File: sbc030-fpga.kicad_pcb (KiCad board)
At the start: 4 copper layers, 152.4 x 114.3 mm, 10 parts, among them J100 C96, U200 74LVC245, U201 74LVC245, U202 74LVC245, U203 74LVC245, U210 74LVC245, U211 74LVC245, U212 74LVC245, U213 74LVC245, U300 LFE5U

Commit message: use LFE5U-12F-8BG256C schematic symbol
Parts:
- U300: value LFE5U -> LFE5U-12F-8BG256C
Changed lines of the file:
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@@
       (effects (font (size 1 1) (thickness 0.15)))
     )
-    (fp_text value LFE5U (at 0 8.2) (layer F.Fab)
+    (fp_text value LFE5U-12F-8BG256C (at 0 8.2) (layer F.Fab)
       (effects (font (size 1 1) (thickness 0.15)))
     )

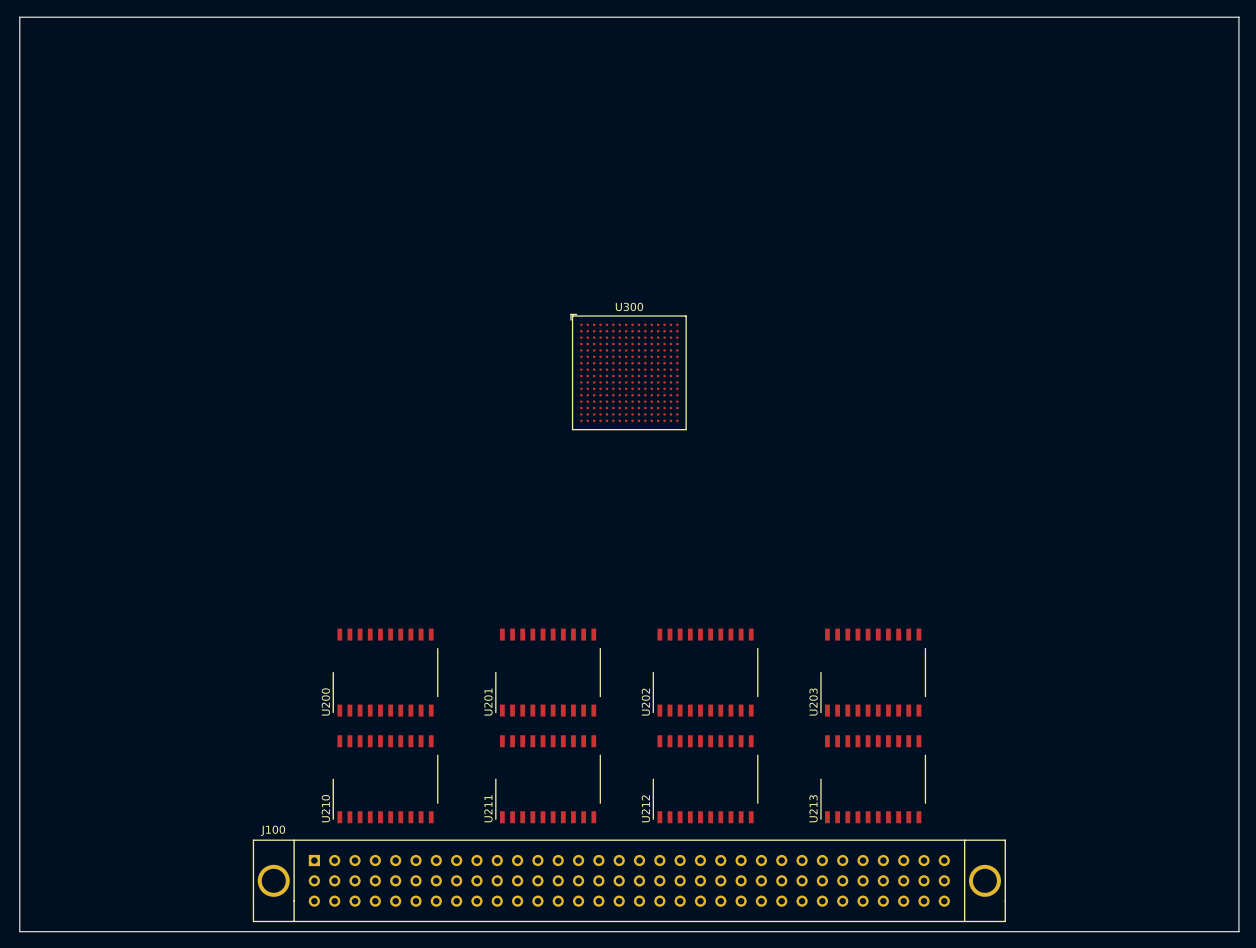
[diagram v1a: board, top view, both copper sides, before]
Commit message: updated schematic and initial bga fanout
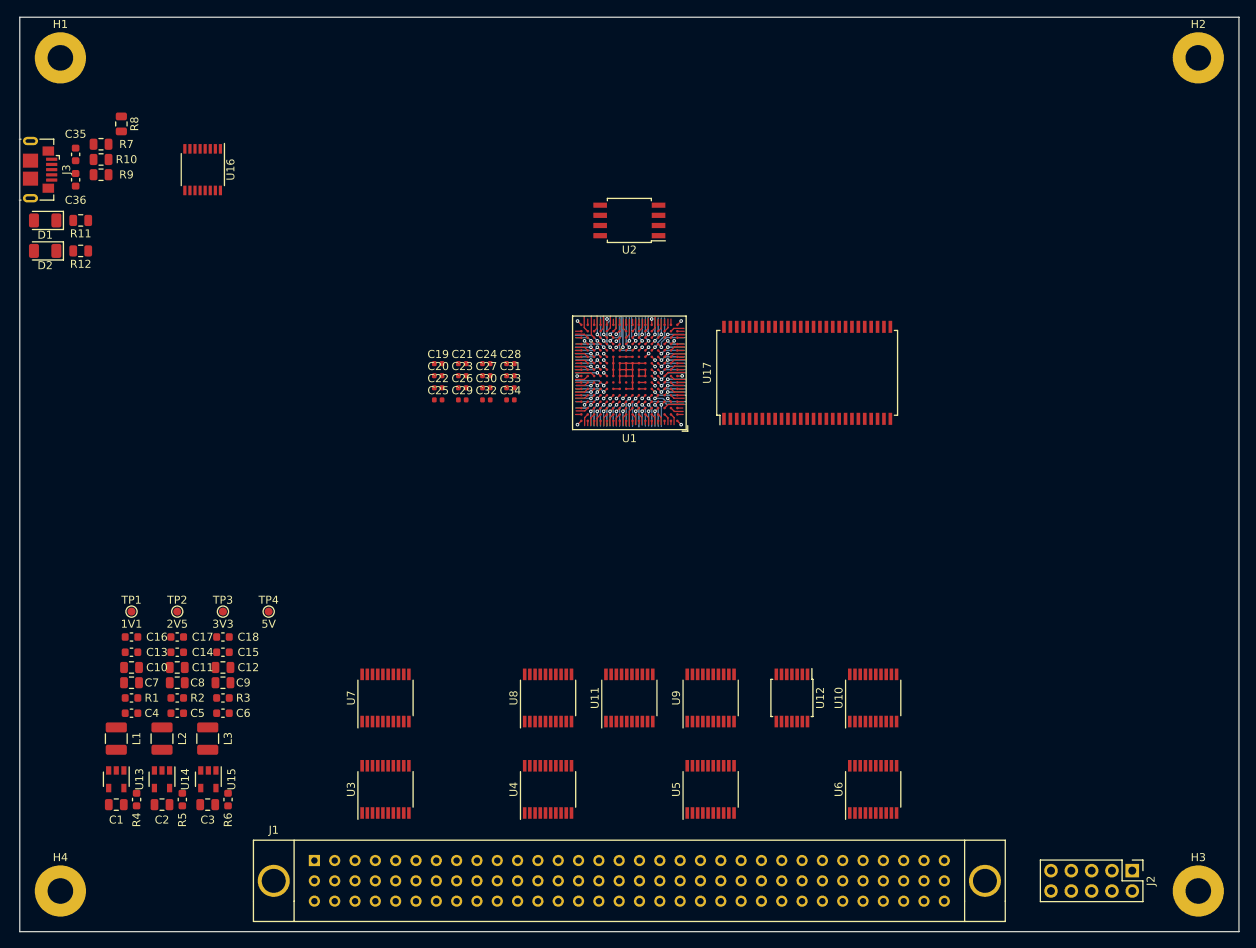
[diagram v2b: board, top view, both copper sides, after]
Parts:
- removed J100: C96, parts:C96ABCM
- removed U200, U201, U202, U203, U210, U211, U212, U213: 74LVC245, Package_SO:SO-20_12.8x7.5mm_P1.27mm
- removed U300: LFE5U-12F-8BG256C, Package_BGA:BGA-256_14.0x14.0mm_Layout16x16_P0.8mm_Ball0.45mm_Pad0.32mm_NSMD
- added C1: 22uF, Capacitor_SMD:C_0805_2012Metric, F.Cu at (81.9, 130.2)
- added C10: 22uF, Capacitor_SMD:C_0805_2012Metric, F.Cu at (83.8, 113.0)
- added C11: 22uF, Capacitor_SMD:C_0805_2012Metric, F.Cu at (89.5, 113.0)
- added C12: 22uF, Capacitor_SMD:C_0805_2012Metric, F.Cu at (95.2, 113.0)
- added C13: 2.2uF, Capacitor_SMD:C_0603_1608Metric, F.Cu at (83.8, 111.1)
- added C14: 2.2uF, Capacitor_SMD:C_0603_1608Metric, F.Cu at (89.5, 111.1)
- added C15: 2.2uF, Capacitor_SMD:C_0603_1608Metric, F.Cu at (95.2, 111.1)
- added C16: 2.2uF, Capacitor_SMD:C_0603_1608Metric, F.Cu at (83.8, 109.2)
- added C17: 2.2uF, Capacitor_SMD:C_0603_1608Metric, F.Cu at (89.5, 109.2)
- added C18: 2.2uF, Capacitor_SMD:C_0603_1608Metric, F.Cu at (95.2, 109.2)
- added C19: 22nF, Capacitor_SMD:C_0402_1005Metric, F.Cu at (122.2, 75.1)
- added C2: 22uF, Capacitor_SMD:C_0805_2012Metric, F.Cu at (87.6, 130.2)
- added C20: 22nF, Capacitor_SMD:C_0402_1005Metric, F.Cu at (122.2, 76.6)
- added C21: 22nF, Capacitor_SMD:C_0402_1005Metric, F.Cu at (125.2, 75.1)
- added C22: 22nF, Capacitor_SMD:C_0402_1005Metric, F.Cu at (122.2, 78.1)
- added C23: 22nF, Capacitor_SMD:C_0402_1005Metric, F.Cu at (125.2, 76.6)
- added C24: 22nF, Capacitor_SMD:C_0402_1005Metric, F.Cu at (128.2, 75.1)
- added C25: 22nF, Capacitor_SMD:C_0402_1005Metric, F.Cu at (122.2, 79.6)
- added C26: 22nF, Capacitor_SMD:C_0402_1005Metric, F.Cu at (125.2, 78.1)
- added C27: 22nF, Capacitor_SMD:C_0402_1005Metric, F.Cu at (128.2, 76.6)
- added C28: 22nF, Capacitor_SMD:C_0402_1005Metric, F.Cu at (131.2, 75.1)
- added C29: 22nF, Capacitor_SMD:C_0402_1005Metric, F.Cu at (125.2, 79.6)
- added C3: 22uF, Capacitor_SMD:C_0805_2012Metric, F.Cu at (93.3, 130.2)
- added C30: 22nF, Capacitor_SMD:C_0402_1005Metric, F.Cu at (128.2, 78.1)
- added C31: 22nF, Capacitor_SMD:C_0402_1005Metric, F.Cu at (131.2, 76.6)
- added C32: 22nF, Capacitor_SMD:C_0402_1005Metric, F.Cu at (128.2, 79.6)
- added C33: 22nF, Capacitor_SMD:C_0402_1005Metric, F.Cu at (131.2, 78.1)
- added C34: 22nF, Capacitor_SMD:C_0402_1005Metric, F.Cu at (131.2, 79.6)
- added C35: 47pF, Capacitor_SMD:C_0603_1608Metric, F.Cu at (76.8, 48.9)
- added C36: 47pF, Capacitor_SMD:C_0603_1608Metric, F.Cu at (76.8, 52.1)
- added C4: 470pF, Capacitor_SMD:C_0603_1608Metric, F.Cu at (83.8, 118.7)
- added C5: 470pF, Capacitor_SMD:C_0603_1608Metric, F.Cu at (89.5, 118.7)
- added C6: 470pF, Capacitor_SMD:C_0603_1608Metric, F.Cu at (95.2, 118.7)
- added C7: 22uF, Capacitor_SMD:C_0805_2012Metric, F.Cu at (83.8, 114.9)
- added C8: 22uF, Capacitor_SMD:C_0805_2012Metric, F.Cu at (89.5, 114.9)
- added C9: 22uF, Capacitor_SMD:C_0805_2012Metric, F.Cu at (95.2, 114.9)
- added D1: LED, LED_SMD:LED_1206_3216Metric, F.Cu at (73.0, 57.1)
- added D2: LED, LED_SMD:LED_1206_3216Metric, F.Cu at (73.0, 61.0)
- added H1: MountingHole, MountingHole:MountingHole_3.2mm_M3, F.Cu at (74.9, 36.8)
- added H2: MountingHole, MountingHole:MountingHole_3.2mm_M3, F.Cu at (217.2, 36.8)
- added H3: MountingHole, MountingHole:MountingHole_3.2mm_M3, F.Cu at (217.2, 141.0)
- added H4: MountingHole, MountingHole:MountingHole_3.2mm_M3, F.Cu at (74.9, 141.0)
- added J1: C96, parts:C96ABCM, F.Cu at (106.7, 137.2)
- added J2: JTAG, Connector_PinHeader_2.54mm:PinHeader_2x05_P2.54mm_Vertical, F.Cu at (208.9, 138.4)
- added J3: USB_B_Micro, Connector_USB:USB_Micro-B_GCT_USB3076-30-A, F.Cu at (72.4, 50.8)
- added L1: 2.2uH, Inductor_SMD:L_1210_3225Metric, F.Cu at (81.9, 121.9)
- added L2: 2.2uH, Inductor_SMD:L_1210_3225Metric, F.Cu at (87.6, 121.9)
- added L3: 2.2uH, Inductor_SMD:L_1210_3225Metric, F.Cu at (93.3, 121.9)
- added R1: 15K, Resistor_SMD:R_0603_1608Metric, F.Cu at (83.8, 116.8)
- added R10: 27R, Resistor_SMD:R_0805_2012Metric, F.Cu at (80.0, 49.5)
- added R11: 10K, Resistor_SMD:R_0805_2012Metric, F.Cu at (77.5, 57.1)
- added R12: 10K, Resistor_SMD:R_0805_2012Metric, F.Cu at (77.5, 61.0)
- added R2: 15K, Resistor_SMD:R_0603_1608Metric, F.Cu at (89.5, 116.8)
- added R3: 15K, Resistor_SMD:R_0603_1608Metric, F.Cu at (95.2, 116.8)
- added R4: 18K, Resistor_SMD:R_0603_1608Metric, F.Cu at (84.5, 129.5)
- added R5: 4.7K, Resistor_SMD:R_0603_1608Metric, F.Cu at (90.2, 129.5)
- added R6: 3.3K, Resistor_SMD:R_0603_1608Metric, F.Cu at (95.9, 129.5)
- added R7: 4.7K, Resistor_SMD:R_0805_2012Metric, F.Cu at (80.0, 47.6)
- added R8: 10K, Resistor_SMD:R_0805_2012Metric, F.Cu at (82.5, 45.1)
- added R9: 27R, Resistor_SMD:R_0805_2012Metric, F.Cu at (80.0, 51.4)
- added TP1: 1V1, TestPoint:TestPoint_Pad_D1.0mm, F.Cu at (83.8, 106.0)
- added TP2: 2V5, TestPoint:TestPoint_Pad_D1.0mm, F.Cu at (89.5, 106.0)
- added TP3: 3V3, TestPoint:TestPoint_Pad_D1.0mm, F.Cu at (95.2, 106.0)
- added TP4: 5V, TestPoint:TestPoint_Pad_D1.0mm, F.Cu at (101.0, 106.0)
- added U1: LFE5U-12F-8BG256C, Package_BGA:BGA-256_14.0x14.0mm_Layout16x16_P0.8mm_Ball0.45mm_Pad0.32mm_NSMD, F.Cu at (146.1, 76.2)
- added U10: 74LVC245, Package_SO:TSSOP-20_4.4x6.5mm_P0.65mm, F.Cu at (176.5, 116.8)
- added U11: 74LVC245, Package_SO:TSSOP-20_4.4x6.5mm_P0.65mm, F.Cu at (146.1, 116.8)
- added U12: TXS0104E, Package_SO:TSSOP-14_4.4x5mm_P0.65mm, F.Cu at (166.4, 116.8)
- added U13: TLV62569DBVR, Package_TO_SOT_SMD:SOT-23-5, F.Cu at (81.9, 127.0)
- added U14: TLV62569DBVR, Package_TO_SOT_SMD:SOT-23-5, F.Cu at (87.6, 127.0)
- added U15: TLV62569DBVR, Package_TO_SOT_SMD:SOT-23-5, F.Cu at (93.4, 127.0)
- added U16: FT230XS, Package_SO:SSOP-16_3.9x4.9mm_P0.635mm, F.Cu at (92.7, 50.8)
- added U17: IS42S16400J-xT, Package_SO:TSOP-II-54_22.2x10.16mm_P0.8mm, F.Cu at (168.3, 76.2)
- added U2: W25Q128JVSIQ, Package_SO:SOIJ-8_5.3x5.3mm_P1.27mm, F.Cu at (146.1, 57.1)
- added U3: 74LVC245, Package_SO:TSSOP-20_4.4x6.5mm_P0.65mm, F.Cu at (115.6, 128.3)
- added U4: 74LVC245, Package_SO:TSSOP-20_4.4x6.5mm_P0.65mm, F.Cu at (135.9, 128.3)
- added U5: 74LVC245, Package_SO:TSSOP-20_4.4x6.5mm_P0.65mm, F.Cu at (156.2, 128.3)
- added U6: 74LVC245, Package_SO:TSSOP-20_4.4x6.5mm_P0.65mm, F.Cu at (176.5, 128.3)
- added U7: 74LVC245, Package_SO:TSSOP-20_4.4x6.5mm_P0.65mm, F.Cu at (115.6, 116.8)
- added U8: 74LVC245, Package_SO:TSSOP-20_4.4x6.5mm_P0.65mm, F.Cu at (135.9, 116.8)
- added U9: 74LVC245, Package_SO:TSSOP-20_4.4x6.5mm_P0.65mm, F.Cu at (156.2, 116.8)
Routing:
- net GND: track 0.00 -> 23.3 mm, vias 0 -> 14
- net +3V3: track 0.00 -> 8.40 mm, vias 0 -> 2
- net Net-(U1-PadM8): track 0.00 -> 6.92 mm, vias 0 -> 1
- net Net-(U1-PadE5): track 0.00 -> 5.43 mm, vias 0 -> 1
- net Net-(U1-PadM11): track 0.00 -> 4.73 mm, vias 0 -> 1
- net Net-(U1-PadM5): track 0.00 -> 4.70 mm, vias 0 -> 1
- net LV_D27: track 0.00 -> 4.60 mm, vias 0 -> 1
- net LV_A20: track 0.00 -> 4.55 mm, vias 0 -> 1
- net Net-(U1-PadM9): track 0.00 -> 4.45 mm, vias 0 -> 1
- net Net-(U1-PadN4): track 0.00 -> 4.34 mm, vias 0 -> 1
- net LV_A12: track 0.00 -> 4.32 mm, vias 0 -> 1
- net /Flash/TDO: track 0.00 -> 4.29 mm, vias 0 -> 1
- net Net-(U1-PadN11): track 0.00 -> 4.25 mm, vias 0 -> 1
- net LV_A11: track 0.00 -> 4.24 mm, vias 0 -> 1
- net Net-(U1-PadM12): track 0.00 -> 4.22 mm, vias 0 -> 1
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- added copper zone on GND, net GND
- removed copper zone on In1.Cu, net GND
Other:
- net class Default: clearance 0.15 -> 0.127; trace_width 0.15 -> 0.095; via_dia 0.6 -> 0.45; via_drill 0.3 -> 0.2
- rule solder_mask_min_width: 0.25 -> 0.025
- rule trace_clearance: 0.15 -> 0.127
- rule trace_min: 0.1 -> 0.09
- rule via_min_drill: 0.3 -> 0.2

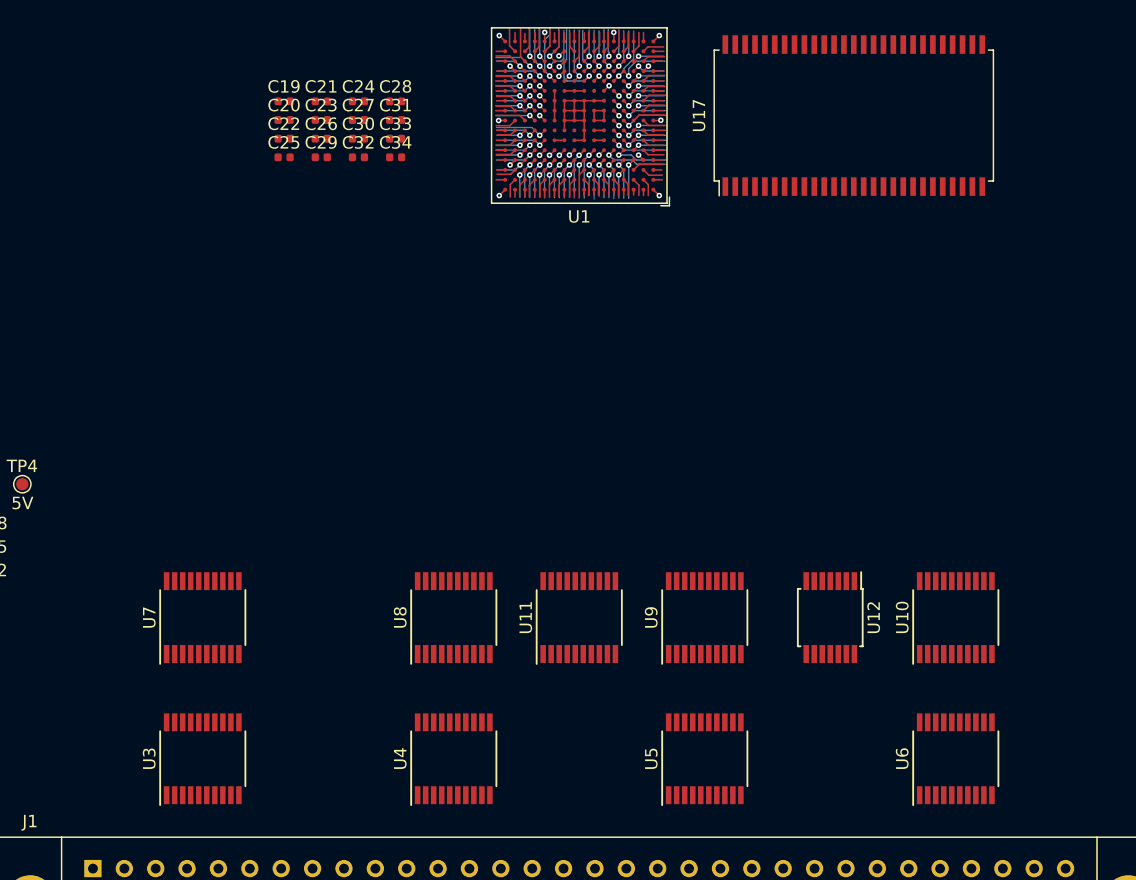
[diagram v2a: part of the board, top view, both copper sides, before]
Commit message: fanout finished and starting work on level translators
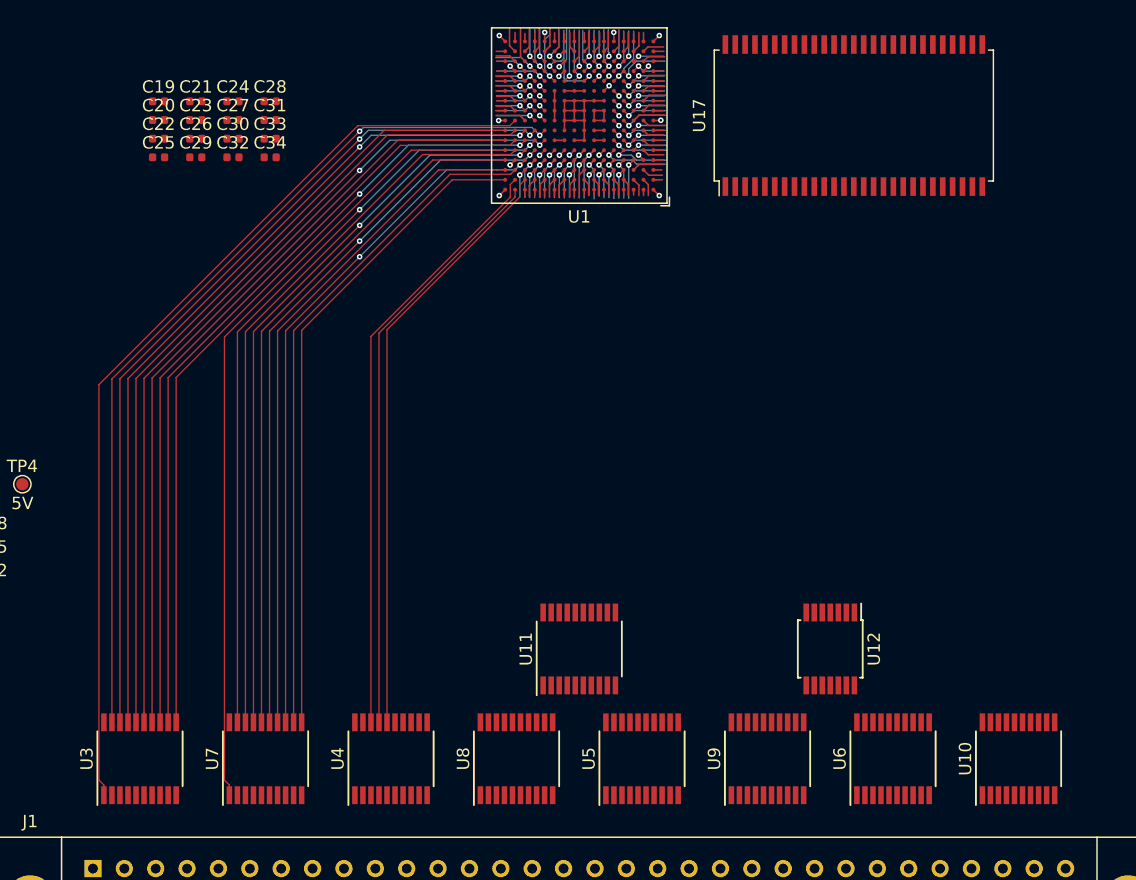
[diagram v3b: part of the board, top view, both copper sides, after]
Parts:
- moved U10 12.5 mm to (181.6, 128.3)
- moved U7 12.5 mm to (120.7, 128.3)
- moved U8 12.5 mm to (141.0, 128.3)
- moved U9 12.5 mm to (161.3, 128.3)
- moved C21 10.2 mm to (115.0, 75.1)
- moved C23 10.2 mm to (115.0, 76.6)
- moved C24 10.2 mm to (118.0, 75.1)
- moved C26 10.2 mm to (115.0, 78.1)
- moved C27 10.2 mm to (118.0, 76.6)
- moved C29 10.2 mm to (115.0, 79.6)
- moved C30 10.2 mm to (118.0, 78.1)
- moved C32 10.2 mm to (118.0, 79.6)
- moved C19 10.2 mm to (112.0, 75.1)
- moved C20 10.2 mm to (112.0, 76.6)
- moved C22 10.2 mm to (112.0, 78.1)
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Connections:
- U1 pad A15: Net-(U1-PadA15) -> LV_A9
- U1 pad B14: Net-(U1-PadB14) -> LV_A10
- U1 pad B15: LV_A1 -> LV_A8
- U1 pad B16: LV_A0 -> LV_D7
- U1 pad B8: LV_D3 -> Net-(U1-PadB8)
- U1 pad B9: LV_D4 -> Net-(U1-PadB9)
- U1 pad C14: LV_A2 -> Net-(U1-PadC14)
- U1 pad C15: LV_A5 -> LV_D6
- U1 pad C16: LV_A4 -> LV_D4
- U1 pad C8: LV_D2 -> Net-(U1-PadC8)
- U1 pad C9: LV_D5 -> Net-(U1-PadC9)
- U1 pad D14: LV_A3 -> LV_D5
- U1 pad D16: LV_A8 -> LV_D2
- U1 pad D8: LV_D1 -> Net-(U1-PadD8)
- U1 pad D9: LV_D6 -> Net-(U1-PadD9)
- U1 pad E13: Net-(U1-PadE13) -> LV_D3
- U1 pad E14: LV_A6 -> LV_D1
- U1 pad E15: LV_A9 -> LV_D0
- U1 pad E16: LV_A15 -> /IO Buffers/DDIR
- U1 pad E8: LV_D0 -> Net-(U1-PadE8)
- U1 pad E9: LV_D7 -> Net-(U1-PadE9)
- U1 pad F12: LV_A11 -> LV_A1
- U1 pad F13: LV_A10 -> /IO Buffers/DOE
- U1 pad F15: LV_A14 -> LV_A6
- U1 pad F16: Net-(U1-PadF16) -> LV_A0
- U1 pad G12: LV_A12 -> /IO Buffers/AOE
- U1 pad G13: LV_A13 -> LV_A5
- U1 pad G14: Net-(U1-PadG14) -> LV_A4
- U1 pad G15: Net-(U1-PadG15) -> LV_A2
- U1 pad G16: Net-(U1-PadG16) -> LV_A3
- U1 pad H15: Net-(U1-PadH15) -> /IO Buffers/ADIR
- U10 pad 16: LV_D26 -> LV_D24
- U10 pad 18: LV_D24 -> LV_D26
- U10 pad 2: D24 -> D26
- U10 pad 4: D26 -> D24
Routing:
- net /IO Buffers/ADIR: track 0.00 -> 75.9 mm
- net /IO Buffers/AOE: track 0.00 -> 71.7 mm, vias 0 -> 2
- net LV_A5: track 1.61 -> 70.1 mm, vias 0 -> 2
- net LV_A4: track 0.69 -> 68.3 mm, vias 0 -> 2
- net LV_A1: track 1.56 -> 68.0 mm, vias 0 -> 2
- net /IO Buffers/DDIR: track 0.00 -> 66.2 mm
- net LV_A2: track 2.39 -> 66.2 mm, vias 1 -> 0
- net LV_A3: track 2.62 -> 66.0 mm, vias 1 -> 0
- net LV_A0: track 0.72 -> 63.8 mm
- net /IO Buffers/DOE: track 0.00 -> 62.1 mm, vias 0 -> 2
- net LV_A7: track 2.51 -> 64.1 mm, vias 1 -> 2
- net LV_A6: track 2.49 -> 63.9 mm, vias 1 -> 0
- net LV_D3: track 1.43 -> 59.2 mm, vias 0 -> 2
- net LV_D1: track 3.23 -> 59.7 mm, vias 1 -> 2
- net LV_D0: track 4.20 -> 59.5 mm, vias 1 -> 0
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
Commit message: level translators done
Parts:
- moved U11 46.6 mm to (100.3, 128.3)
- moved U12 26.3 mm to (191.1, 128.3)
- moved C1 6.98 mm to (74.9, 130.2)
- moved C10 6.98 mm to (76.8, 113.0)
- moved C11 6.98 mm to (82.5, 113.0)
- moved C12 6.98 mm to (88.3, 113.0)
- moved C13 6.98 mm to (76.8, 111.1)
- moved C14 6.98 mm to (82.5, 111.1)
- moved C15 6.98 mm to (88.3, 111.1)
- moved C16 6.98 mm to (76.8, 109.2)
- moved C17 6.98 mm to (82.5, 109.2)
- moved C18 6.98 mm to (88.3, 109.2)
- moved C2 6.98 mm to (80.6, 130.2)
- moved C3 6.98 mm to (86.4, 130.2)
- moved C4 6.98 mm to (76.8, 118.7)
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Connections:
- U1 pad A10: LV_D9 -> LV_A21
- U1 pad A11: LV_D18 -> LV_A17
- U1 pad A12: LV_D19 -> LV_D13
- U1 pad A13: Net-(U1-PadA13) -> LV_D9
- U1 pad A14: Net-(U1-PadA14) -> LV_A12
- U1 pad A2: LV_A16 -> LV_RESET
- U1 pad A3: LV_A18 -> LV_D31
- U1 pad A4: LV_A19 -> LV_D29
- U1 pad A5: Net-(U1-PadA5) -> LV_D25
- U1 pad A6: Net-(U1-PadA6) -> LV_A29
- U1 pad A7: Net-(U1-PadA7) -> LV_A25
- U1 pad A8: Net-(U1-PadA8) -> LV_D21
- U1 pad A9: LV_D8 -> LV_D17
- U1 pad B1: LV_A24 -> Net-(U1-PadB1)
- U1 pad B10: LV_D10 -> LV_A19
- U1 pad B11: LV_D14 -> LV_D15
- U1 pad B12: LV_D20 -> LV_D11
- U1 pad B13: Net-(U1-PadB13) -> LV_A14
- U1 pad B2: LV_A25 -> Net-(U1-PadB2)
- U1 pad B3: LV_A17 -> LV_MIRQ
- U1 pad B4: LV_A23 -> LV_D30
- U1 pad B5: Net-(U1-PadB5) -> LV_D27
- U1 pad B6: Net-(U1-PadB6) -> LV_A31
- U1 pad B7: Net-(U1-PadB7) -> LV_A27
- U1 pad B8: Net-(U1-PadB8) -> LV_D23
- U1 pad B9: Net-(U1-PadB9) -> LV_A23
- U1 pad C1: LV_A28 -> Net-(U1-PadC1)
- U1 pad C10: LV_D11 -> LV_A18
- U1 pad C11: LV_D15 -> LV_D14
- U1 pad C12: LV_D21 -> LV_D10
- U1 pad C13: Net-(U1-PadC13) -> LV_A15
- U1 pad C14: Net-(U1-PadC14) -> LV_A11
- U1 pad C2: LV_A29 -> Net-(U1-PadC2)
- U1 pad C3: LV_A26 -> Net-(U1-PadC3)
- U1 pad C4: LV_A22 -> LV_D24
- U1 pad C5: Net-(U1-PadC5) -> LV_A30
- U1 pad C6: Net-(U1-PadC6) -> LV_A26
- U1 pad C7: Net-(U1-PadC7) -> LV_D22
- U1 pad C8: Net-(U1-PadC8) -> LV_D19
- U1 pad C9: Net-(U1-PadC9) -> LV_A22
- U1 pad D1: LV_D24 -> Net-(U1-PadD1)
- U1 pad D10: LV_D12 -> LV_A16
- U1 pad D11: LV_D16 -> LV_D12
- U1 pad D12: LV_D22 -> LV_D8
- U1 pad D13: Net-(U1-PadD13) -> LV_A13
- U1 pad D3: LV_A27 -> Net-(U1-PadD3)
- U1 pad D4: LV_A21 -> LV_D28
- U1 pad D5: Net-(U1-PadD5) -> LV_D26
- U1 pad D6: Net-(U1-PadD6) -> LV_A28
- U1 pad D7: Net-(U1-PadD7) -> LV_A24
- U1 pad D8: Net-(U1-PadD8) -> LV_D18
- U1 pad D9: Net-(U1-PadD9) -> LV_A20
- U1 pad E1: LV_D31 -> Net-(U1-PadE1)
- U1 pad E10: LV_D13 -> Net-(U1-PadE10)
- U1 pad E11: LV_D17 -> Net-(U1-PadE11)
- U1 pad E12: LV_D23 -> Net-(U1-PadE12)
- U1 pad E2: LV_D25 -> Net-(U1-PadE2)
- U1 pad E3: LV_A30 -> Net-(U1-PadE3)
- U1 pad E4: LV_A20 -> LV_DSACK0
- U1 pad E5: Net-(U1-PadE5) -> LV_DSACK1
- U1 pad E7: Net-(U1-PadE7) -> LV_D20
- U1 pad E8: Net-(U1-PadE8) -> LV_D16
- U1 pad F2: LV_D30 -> Net-(U1-PadF2)
- U1 pad F3: LV_A31 -> Net-(U1-PadF3)
- U1 pad F4: LV_D26 -> Net-(U1-PadF4)
- U1 pad F5: LV_D27 -> Net-(U1-PadF5)
- U1 pad G4: LV_D29 -> Net-(U1-PadG4)
- U1 pad G5: LV_D28 -> Net-(U1-PadG5)
- U1 pad H13: Net-(U1-PadH13) -> LV_FC0
- U1 pad H14: Net-(U1-PadH14) -> LV_RW
- U1 pad J13: Net-(U1-PadJ13) -> LV_AS
- U1 pad J14: Net-(U1-PadJ14) -> LV_SIZ0
- U1 pad J15: Net-(U1-PadJ15) -> LV_DS
- U1 pad J16: Net-(U1-PadJ16) -> LV_FC1
- U1 pad K14: Net-(U1-PadK14) -> /IO Buffers/CDIR
- U1 pad K15: Net-(U1-PadK15) -> /IO Buffers/COE
- U1 pad K16: Net-(U1-PadK16) -> LV_SIZ1
- U11 pad 11: LV_SIZ1 -> LV_RW
- U11 pad 12: LV_SIZ0 -> LV_FC0
- U11 pad 13: LV_DS -> LV_FC1
- U11 pad 15: LV_FC1 -> LV_DS
- U11 pad 16: LV_FC0 -> LV_SIZ0
- U11 pad 17: LV_RW -> LV_SIZ1
- U11 pad 3: RW -> SIZ1
- U11 pad 4: FC0 -> SIZ0
- U11 pad 5: FC1 -> DS
- U11 pad 7: DS -> FC1
- U11 pad 8: SIZ0 -> FC0
- U11 pad 9: SIZ1 -> RW
- U12 pad 10: DSACK0 -> MIRQ
- U12 pad 11: RESET -> DSACK1
- U12 pad 12: DSACK1 -> RESET
- U12 pad 13: MIRQ -> DSACK0
- U12 pad 2: LV_MIRQ -> LV_DSACK0
- U12 pad 3: LV_DSACK1 -> LV_RESET
- U12 pad 4: LV_RESET -> LV_DSACK1
- U12 pad 5: LV_DSACK0 -> LV_MIRQ
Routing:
- net DSACK0: track 0.00 -> 95.1 mm, vias 0 -> 1
- net SIZ1: track 0.00 -> 94.4 mm
- net SIZ0: track 0.00 -> 91.3 mm
- net RESET: track 0.00 -> 89.1 mm, vias 0 -> 1
- net /IO Buffers/CDIR: track 0.00 -> 83.6 mm, vias 0 -> 2
- net DS: track 0.00 -> 77.8 mm
- net /IO Buffers/COE: track 0.00 -> 75.8 mm
- net LV_SIZ0: track 0.00 -> 74.7 mm, vias 0 -> 2
- net LV_AS: track 0.00 -> 74.2 mm, vias 0 -> 2
- net LV_SIZ1: track 0.00 -> 73.7 mm
- net LV_DS: track 0.00 -> 73.2 mm
- net AS: track 0.00 -> 73.1 mm
- net LV_FC0: track 0.00 -> 72.6 mm, vias 0 -> 2
- net LV_RW: track 0.00 -> 71.2 mm
- net LV_FC1: track 0.00 -> 70.8 mm
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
